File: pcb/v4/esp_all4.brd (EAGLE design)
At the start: 45 x 95 mm, 31 parts, among them IC1 4000D, Q1 BUZ11BH

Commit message: added v4, with i2c
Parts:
- added R2, R3: 4.7k, rcl:M0805
- added SV4: (no value), con-lstb:MA04-1
- moved U$4 87.0 mm to (9.10, 80.7)
- moved U$9 72.9 mm to (8.90, 72.4)
- moved U$11 60.7 mm to (2.00, 78.0)
- moved U$1 52.4 mm to (24.1, 53.0)
- moved SV1 4.01 mm to (5.60, 86.9)
- renumbered DIMMING to T_DIM1, DIMMING1 to T_DIM2, DIMMING2 to T_DIM3, U$12 to DP3, U$13 to DP2
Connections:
- removed net DHT_SIG: DHT22.2, ESP.D4, ESP.D41
- removed net NOT: ESP.D3, ESP.D31, IC1.4
- new net DHT_SIG/SDA: DHT22.2, ESP.D4, ESP.D41, SV4.2
- new net N$3: R2.2, R3.2, T_DIM3.2, T_DIM3.4
- new net SCL: ESP.D5, ESP.D51, SV4.1
- net DIMMING3: now also R3.1; no longer T_DIM3.2, T_DIM3.4
- net GND: now also R2.1, SV4.3
- net PIR: now also ESP.D3, ESP.D31; no longer ESP.D5, ESP.D51
- net VDD: now also SV4.4
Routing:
- net DHT_SIG/SDA: track 0.00 -> 138.4 mm, vias 0 -> 2
- net SCL: track 0.00 -> 82.5 mm, vias 0 -> 2
- net DHT_SIG: track 49.1 -> 0.00 mm, vias 1 -> 0
- net NOT: track 35.2 -> 0.00 mm, vias 2 -> 0
- net N$3: track 0.00 -> 20.7 mm, vias 0 -> 1
- net DIMMING3: track 24.3 -> 8.45 mm
- net PIR: track 68.5 -> 58.3 mm
- net DIMM1: track 96.7 -> 104.4 mm
- net VDD: track 189.9 -> 195.1 mm
- net ONEWIRE_DS12B20: track 98.1 -> 94.0 mm
- net RELAY_LO3: track 31.9 -> 35.4 mm, vias 0 -> 2
- net GND: track 58.2 -> 54.9 mm
- net DIMM3: track 60.2 -> 61.5 mm
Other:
- board text added: "DIM1"
- board text added: "DIM2"
- board text added: "DIM3"
- board text removed: "DIMM1"

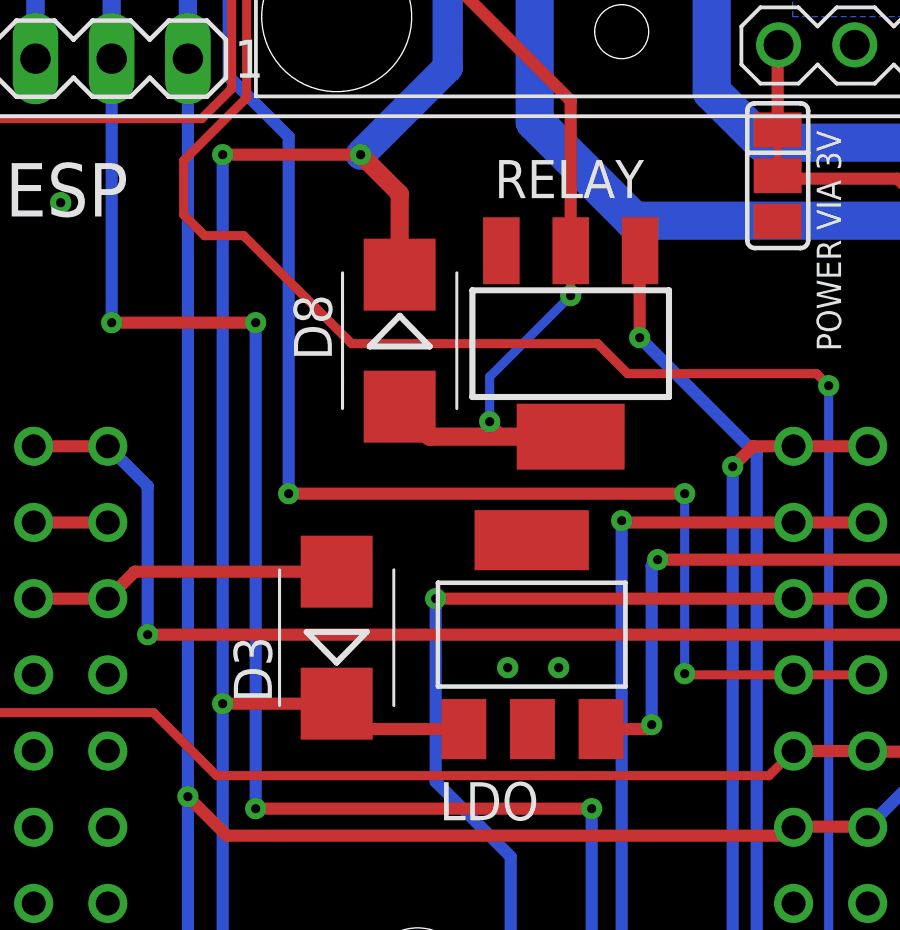
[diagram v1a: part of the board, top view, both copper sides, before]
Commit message: fixed LDO
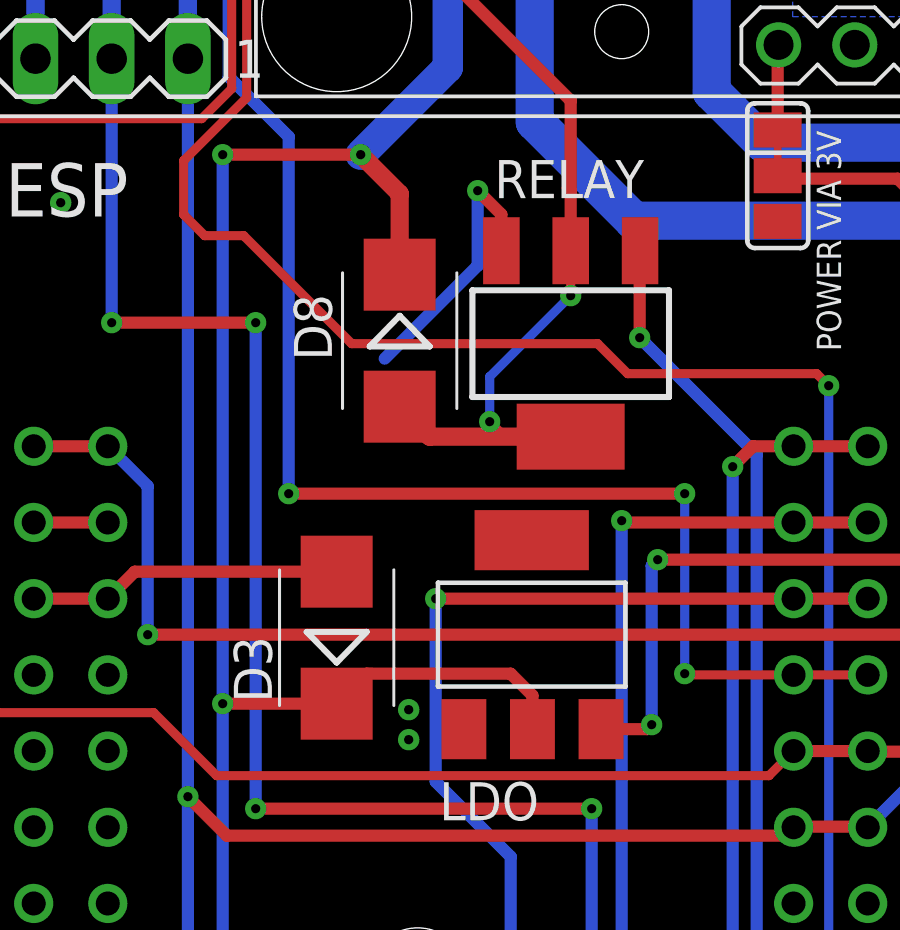
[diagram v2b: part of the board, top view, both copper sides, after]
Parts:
- LDO: value REG1118 -> REG1117
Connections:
- net GND: now also LDO.1; no longer LDO.2
- net VCC: now also LDO.2; no longer LDO.1
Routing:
- net GND: track 54.9 -> 64.1 mm, vias 14 -> 15
- net VCC: track 97.6 -> 102.6 mm
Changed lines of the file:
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@@
 <element name="U$11" library="JKW_CHIP" package="LOGO2_10X10_SILK" value="LOGO_10X10_SILK" x="2" y="78"/>
 <element name="D3" library="diode" package="SMB" value="ES2D" x="13.4" y="44.2" rot="R90"/>
-<element name="LDO" library="burr-brown" package="SOT223" value="REG1118" x="19.9" y="44.3" smashed="yes">
-<attribute name="MPN" value="REG1118-2.85/2K5G4" x="19.9" y="44.3" size="1.778" layer="27" display="off"/>
-<attribute name="OC_NEWARK" value="14M2185" x="19.9" y="44.3" size="1.778" layer="27" display="off"/>
-<attribute name="OC_FARNELL" value="unknown" x="19.9" y="44.3" size="1.778" layer="27" display="off"/>
+<element name="LDO" library="burr-brown" package="SOT223" value="REG1117" x="19.9" y="44.3" smashed="yes">
+<attribute name="MPN" value="REG1117" x="19.9" y="44.3" size="1.778" layer="27" display="off"/>
+<attribute name="OC_NEWARK" value="14P6981" x="19.9" y="44.3" size="1.778" layer="27" display="off"/>
+<attribute name="OC_FARNELL" value="1097566" x="19.9" y="44.3" size="1.778" layer="27" display="off"/>
 <attribute name="MF" value="" x="19.9" y="44.3" size="1.778" layer="27" display="off"/>
 <attribute name="NAME" x="20.14" y="39.382" size="1.27" layer="25" font="vector" ratio="10" rot="R180"/>
@@
 <contactref element="ESP" pad="GND@7"/>
 <wire x1="3.36" y1="67" x2="3.36" y2="63.5" width="0.6096" layer="16"/>
-<contactref element="LDO" pad="2"/>
+<contactref element="LDO" pad="1"/>
 <via x="4.2" y="58.7" extent="1-16" drill="0.3084"/>
 <contactref element="Q1" pad="S"/>
@@
 <via x="24.1" y="9.9" extent="1-16" drill="0.3084"/>
 <via x="24.1" y="8.6" extent="1-16" drill="0.3084"/>
-<via x="19.1" y="43.2" extent="1-16" drill="0.3084"/>
-<via x="20.8" y="43.2" extent="1-16" drill="0.3084"/>
+<via x="15.8" y="40.8" extent="1-16" drill="0.3084"/>
+<via x="15.8" y="41.8" extent="1-16" drill="0.3084"/>
 <contactref element="U$10" pad="P$2"/>
 <contactref element="R2" pad="1"/>
@@
 <wire x1="4.2" y1="89.8" x2="4.2" y2="92.17" width="0.6096" layer="16"/>
 <wire x1="4.2" y1="92.17" x2="4.23" y2="92.2" width="0.6096" layer="16"/>
-<wire x1="18.889" y1="57.099" x2="19.1" y2="43.2" width="0" layer="19" extent="1-1"/>
+<wire x1="18.889" y1="57.099" x2="18.889" y2="58.311" width="0.4064" layer="1"/>
+<wire x1="18.889" y1="58.311" x2="18.1" y2="59.1" width="0.4064" layer="1"/>
+<via x="18.1" y="59.1" extent="1-16" drill="0.3048"/>
+<wire x1="18.1" y1="59.1" x2="18.1" y2="56.6" width="0.4064" layer="16"/>
+<wire x1="18.1" y1="56.6" x2="15" y2="53.5" width="0.4064" layer="16"/>
 </signal>
 <signal name="VCC">
@@
 <wire x1="18.6" y1="74.9" x2="17.9" y2="75.6" width="0.8128" layer="1"/>
 <wire x1="17.9" y1="75.6" x2="17.9" y2="77.8" width="0.8128" layer="1"/>
-<contactref element="LDO" pad="1"/>
+<contactref element="LDO" pad="2"/>
 <wire x1="17.1" y1="73.4" x2="17.1" y2="63.2" width="1.016" layer="16"/>
 <wire x1="17.1" y1="63.2" x2="14.2" y2="60.3" width="1.016" layer="16"/>
@@
 <wire x1="15.5" y1="56.3" x2="15.5" y2="59" width="0.6096" layer="1"/>
 <wire x1="15.5" y1="59" x2="14.2" y2="60.3" width="0.6096" layer="1"/>
-<wire x1="17.6394" y1="41.1504" x2="14.2496" y2="41.1504" width="0.4064" layer="1"/>
 <wire x1="14.2496" y1="41.1504" x2="13.4" y2="42" width="0.4064" layer="1"/>
 <wire x1="13.4" y1="42" x2="9.6" y2="42" width="0.4064" layer="1"/>
@@
 <via x="9.6" y="60.3" extent="1-16" drill="0.3048"/>
 <wire x1="9.6" y1="60.3" x2="14.2" y2="60.3" width="0.4064" layer="1"/>
+<wire x1="19.9254" y1="41.1504" x2="19.9254" y2="42.2746" width="0.4064" layer="1"/>
+<wire x1="19.9254" y1="42.2746" x2="19.2" y2="43" width="0.4064" layer="1"/>
+<wire x1="19.2" y1="43" x2="14.4" y2="43" width="0.4064" layer="1"/>
+<wire x1="14.4" y1="43" x2="13.4" y2="42" width="0.4064" layer="1"/>
 </signal>
 <signal name="RELAY_LO3">

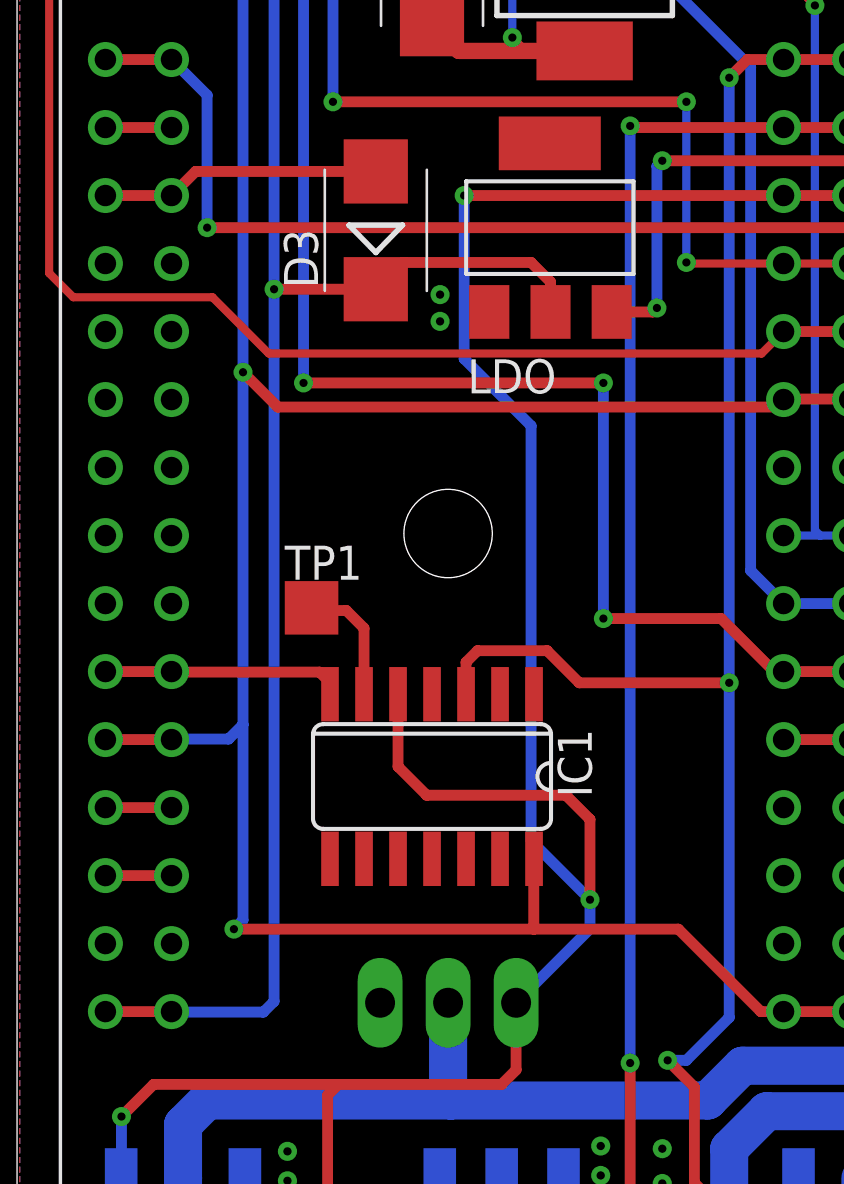
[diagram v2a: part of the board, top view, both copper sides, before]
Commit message: added voltage reg
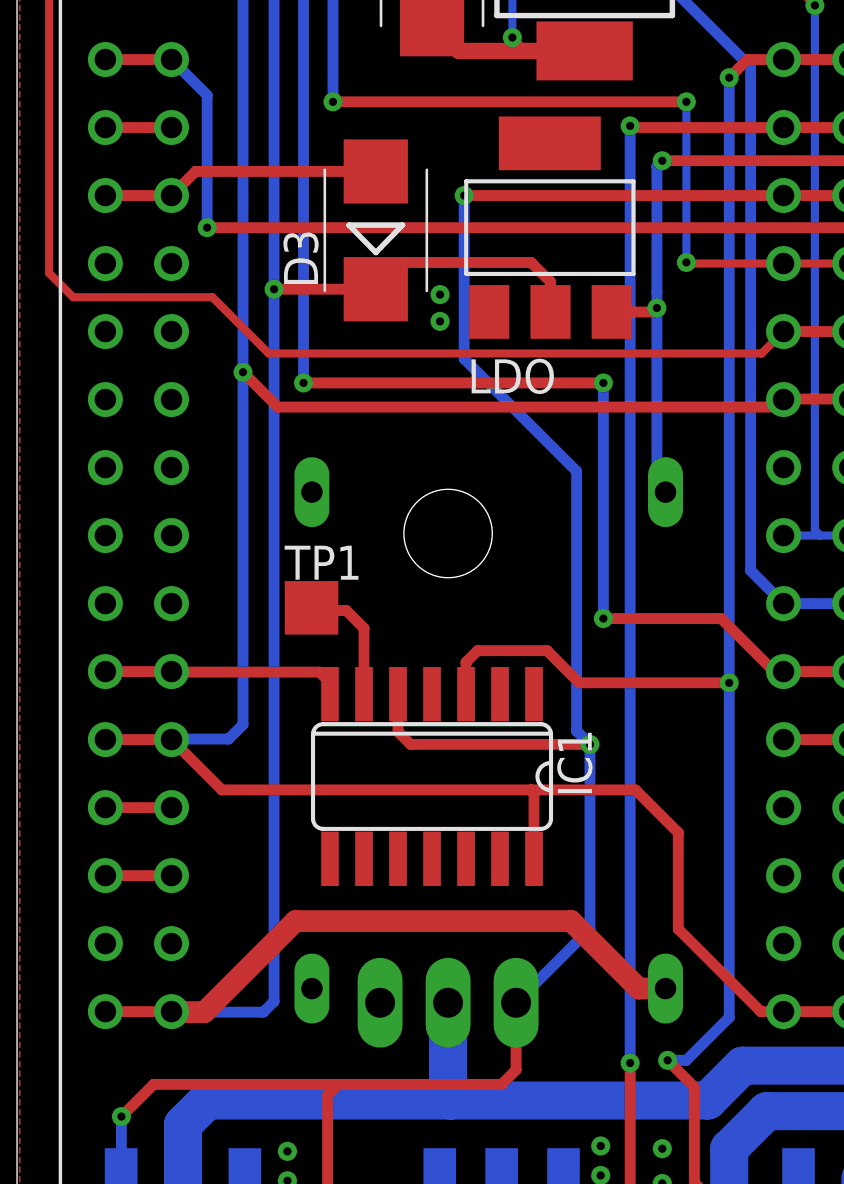
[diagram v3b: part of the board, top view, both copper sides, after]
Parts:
- added U$12: MP1584EN_FRAMELESS, JKW_CHIP:MP1584EN_FRAMELESS
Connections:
- net GND: now also U$12.GNDIN, U$12.GNDOUT
- net N$17: now also U$12.VIN
- net VCC: now also U$12.VOUT
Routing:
- net VCC: track 102.6 -> 123.5 mm
- net N$17: track 23.2 -> 30.4 mm
- net DIMM1: track 104.4 -> 99.5 mm
- net VDD: track 195.1 -> 194.7 mm, vias 4 -> 3
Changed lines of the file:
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@@
 <?xml version="1.0" encoding="utf-8"?>
 <!DOCTYPE eagle SYSTEM "eagle.dtd">
-<eagle version="7.6.0">
+<eagle version="7.7.0">
 <drawing>
 <settings>
@@
 <attribute name="MPN" value="" x="5.5" y="92.2" size="1.778" layer="27" rot="R180" display="off"/>
 </element>
+<element name="U$12" library="JKW_CHIP" package="MP1584EN_FRAMELESS" value="MP1584EN_FRAMELESS" x="26" y="36.2" rot="MR270"/>
 </elements>
 <signals>
@@
 <via x="16.7" y="45.5" extent="1-16" drill="0.3048"/>
 <wire x1="16.7" y1="45.5" x2="16.7" y2="39.4" width="0.4064" layer="16"/>
-<wire x1="16.7" y1="39.4" x2="19.2" y2="36.9" width="0.4064" layer="16"/>
-<wire x1="19.2" y1="36.9" x2="19.2" y2="21.4" width="0.4064" layer="16"/>
+<wire x1="16.7" y1="39.4" x2="20.9" y2="35.2" width="0.4064" layer="16"/>
 <wire x1="26.6" y1="4.276" x2="13.4" y2="4.276" width="0.4064" layer="1"/>
 <via x="3.9" y="11.1" extent="1-16" drill="0.3048"/>
@@
 <wire x1="12" y1="12.3" x2="5.1" y2="12.3" width="0.4064" layer="1"/>
 <wire x1="5.1" y1="12.3" x2="3.9" y2="11.1" width="0.4064" layer="1"/>
-<wire x1="14.23" y1="26.8734" x2="14.23" y2="24.17" width="0.4064" layer="1"/>
 <wire x1="13.4" y1="4.276" x2="12.224" y2="4.276" width="0.4064" layer="1"/>
 <wire x1="12.224" y1="4.276" x2="11.6" y2="4.9" width="0.4064" layer="1"/>
@@
 <wire x1="11.6" y1="11.9" x2="12" y2="12.3" width="0.4064" layer="1"/>
 <wire x1="18.64" y1="15.35" x2="21.4" y2="18.11" width="0.4064" layer="16"/>
-<wire x1="21.4" y1="18.11" x2="21.4" y2="19.2" width="0.4064" layer="16"/>
-<wire x1="21.4" y1="19.2" x2="19.2" y2="21.4" width="0.4064" layer="16"/>
-<wire x1="14.23" y1="24.17" x2="15.3" y2="23.1" width="0.4064" layer="1"/>
-<wire x1="15.3" y1="23.1" x2="20.5" y2="23.1" width="0.4064" layer="1"/>
-<wire x1="20.5" y1="23.1" x2="21.4" y2="22.2" width="0.4064" layer="1"/>
-<wire x1="21.4" y1="22.2" x2="21.4" y2="19.2" width="0.4064" layer="1"/>
-<via x="21.4" y="19.2" extent="1-16" drill="0.3048"/>
+<wire x1="14.23" y1="26.8734" x2="14.23" y2="25.47" width="0.4064" layer="1"/>
+<wire x1="14.23" y1="25.47" x2="14.7" y2="25" width="0.4064" layer="1"/>
+<wire x1="14.7" y1="25" x2="21.4" y2="25" width="0.4064" layer="1"/>
+<via x="21.4" y="25" extent="1-16" drill="0.3048"/>
+<wire x1="21.4" y1="25" x2="21.4" y2="18.11" width="0.4064" layer="16"/>
+<wire x1="20.9" y1="35.2" x2="20.9" y2="25.5" width="0.4064" layer="16"/>
+<wire x1="20.9" y1="25.5" x2="21.4" y2="25" width="0.4064" layer="16"/>
 </signal>
 <signal name="DIMM3">
@@
 <wire x1="18.1" y1="59.1" x2="18.1" y2="56.6" width="0.4064" layer="16"/>
 <wire x1="18.1" y1="56.6" x2="15" y2="53.5" width="0.4064" layer="16"/>
+<contactref element="U$12" pad="GNDIN"/>
+<contactref element="U$12" pad="GNDOUT"/>
+<wire x1="24.1" y1="8.6" x2="31.5" y2="4.05" width="0" layer="19" extent="1-1"/>
 </signal>
 <signal name="VCC">
@@
 <wire x1="19.2" y1="43" x2="14.4" y2="43" width="0.4064" layer="1"/>
 <wire x1="14.4" y1="43" x2="13.4" y2="42" width="0.4064" layer="1"/>
+<contactref element="U$12" pad="VOUT"/>
+<wire x1="24.222" y1="15.88" x2="23.22" y2="15.88" width="0.8128" layer="1"/>
+<wire x1="23.22" y1="15.88" x2="20.7" y2="18.4" width="0.8128" layer="1"/>
+<wire x1="20.7" y1="18.4" x2="10.4" y2="18.4" width="0.8128" layer="1"/>
+<wire x1="10.4" y1="18.4" x2="7" y2="15" width="0.8128" layer="1"/>
+<wire x1="7" y1="15" x2="5.79" y2="15" width="0.8128" layer="1"/>
+<wire x1="5.79" y1="15" x2="5.77" y2="15.02" width="0.8128" layer="1"/>
 </signal>
 <signal name="RELAY_LO3">
@@
 <wire x1="23.7504" y1="41.1504" x2="23.9" y2="41.3" width="0.4064" layer="1"/>
 <via x="23.9" y="41.3" extent="1-16" drill="0.3048"/>
-<wire x1="23.9" y1="41.3" x2="23.9" y2="46.6" width="0.4064" layer="16"/>
+<wire x1="23.9" y1="41.3" x2="23.9" y2="41.9" width="0.4064" layer="16"/>
+<wire x1="23.9" y1="41.9" x2="23.9" y2="46.6" width="0.4064" layer="16"/>
 <wire x1="23.9" y1="46.6" x2="24.1" y2="46.8" width="0.4064" layer="16"/>
 <via x="24.1" y="46.8" extent="1-16" drill="0.3048"/>
@@
 <wire x1="33.7" y1="46.8" x2="34.9" y2="48" width="0.4064" layer="1"/>
 <wire x1="34.9" y1="48" x2="39.5" y2="48" width="0.4064" layer="1"/>
+<contactref element="U$12" pad="VIN"/>
+<wire x1="24.222" y1="34.422" x2="23.9" y2="34.422" width="0.4064" layer="16"/>
+<wire x1="23.9" y1="34.422" x2="23.9" y2="41.3" width="0.4064" layer="16"/>
 </signal>
 <signal name="VDD">
@@
 <via x="8.44" y="38.9" extent="1-16" drill="0.3048"/>
 <wire x1="27.78" y1="15.02" x2="24.7" y2="18.1" width="0.4064" layer="1"/>
-<wire x1="24.7" y1="18.1" x2="19.3" y2="18.1" width="0.4064" layer="1"/>
-<via x="8.1" y="18.1" extent="1-16" drill="0.3048"/>
-<wire x1="19.3" y1="18.1" x2="8.1" y2="18.1" width="0.4064" layer="1"/>
-<wire x1="8.1" y1="18.1" x2="8.44" y2="18.44" width="0.4064" layer="16"/>
-<wire x1="8.44" y1="18.44" x2="8.44" y2="25.74" width="0.4064" layer="16"/>
 <wire x1="40.08" y1="15.02" x2="31.1" y2="15.02" width="0.4064" layer="1"/>
 <wire x1="19.31" y1="20.7266" x2="19.3" y2="20.7166" width="0.4064" layer="1"/>
-<wire x1="19.3" y1="20.7166" x2="19.3" y2="18.1" width="0.4064" layer="1"/>
 <contactref element="ESP" pad="3V3@2"/>
 <contactref element="ESP" pad="3V3@1"/>
@@
 <wire x1="8.1" y1="88.6" x2="8.1" y2="86.94" width="0.6096" layer="1"/>
 <wire x1="8.1" y1="86.94" x2="8.14" y2="86.9" width="0.6096" layer="1"/>
+<wire x1="24.7" y1="18.1" x2="24.7" y2="21.7" width="0.4064" layer="1"/>
+<wire x1="24.7" y1="21.7" x2="23.1" y2="23.3" width="0.4064" layer="1"/>
+<wire x1="23.1" y1="23.3" x2="19.2" y2="23.3" width="0.4064" layer="1"/>
+<wire x1="19.2" y1="23.3" x2="7.65" y2="23.3" width="0.4064" layer="1"/>
+<wire x1="7.65" y1="23.3" x2="5.77" y2="25.18" width="0.4064" layer="1"/>
+<wire x1="19.31" y1="20.7266" x2="19.31" y2="23.19" width="0.4064" layer="1"/>
+<wire x1="19.31" y1="23.19" x2="19.2" y2="23.3" width="0.4064" layer="1"/>
 </signal>
 <signal name="DIMMING2">
